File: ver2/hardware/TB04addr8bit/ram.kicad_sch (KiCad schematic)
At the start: 5 parts, among them U29 6116, U32 74AHC04, U40 74HC00, U43 74LS08

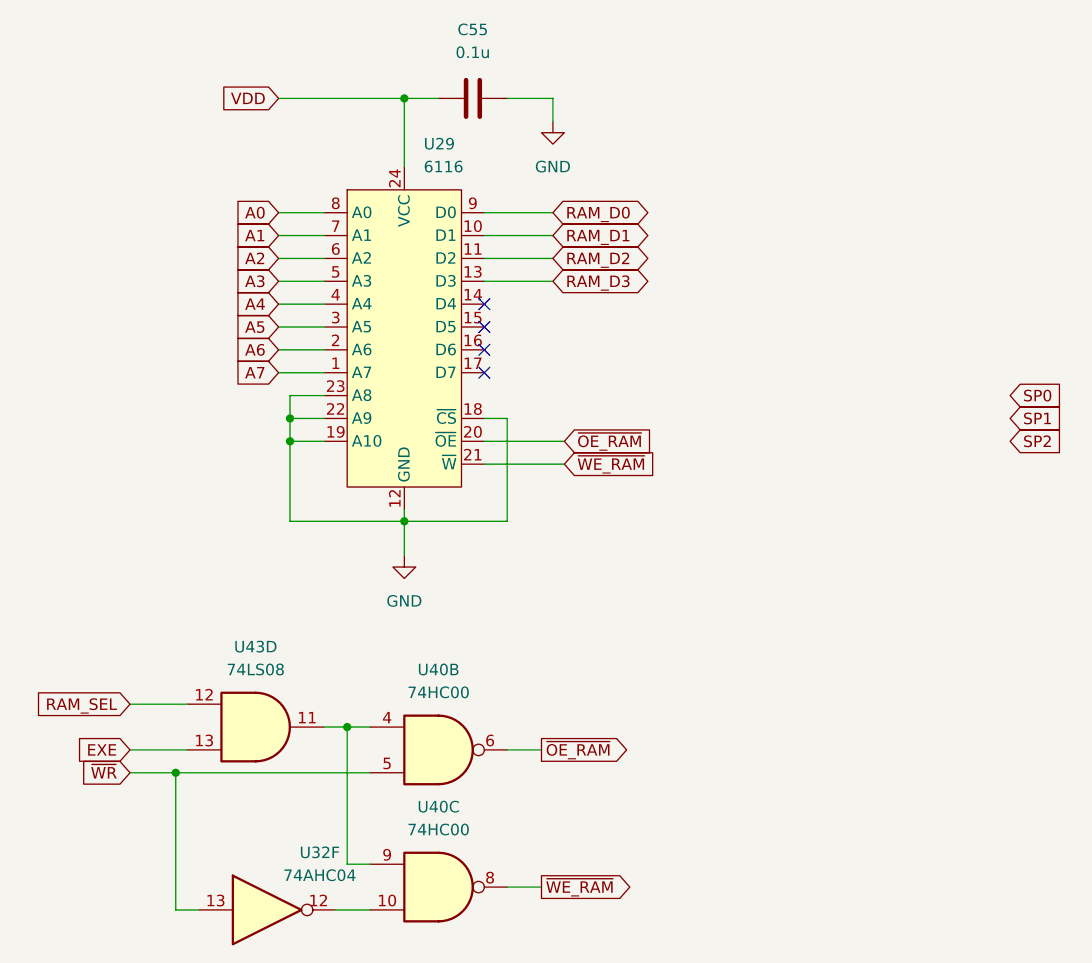
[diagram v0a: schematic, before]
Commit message: ver2: 回路図の要修正5件を修正しアノテーションを掛け直し
- 74HC193(旧U39/新U38)の~CO・~BOをVDD直結から開放に(出力短絡の回避)
- 電源未接続だった4IC(74HC00/74LS32/74AHC04/74LS08)にVCC/GNDを配線
  し、バイパスコンデンサ0.1u×4を追加
- ネット名 Decord を DCR に統一(デコーダ制御信号のラッチ不成立を解消)
- PC_LAOD の綴りを PC_LOAD に修正
- 書込デコーダ138の入力を OPR8-10 から sel_a0-2 へ付け替え
  (LD Ri,[Im8] が別レジスタに書く不具合の解消)
- ver1基板由来だった参照記号をアノテーション掛け直しで整理
  (部品216個・名前付きネット146本とも掛け直し前後で一致、ERCも同数)
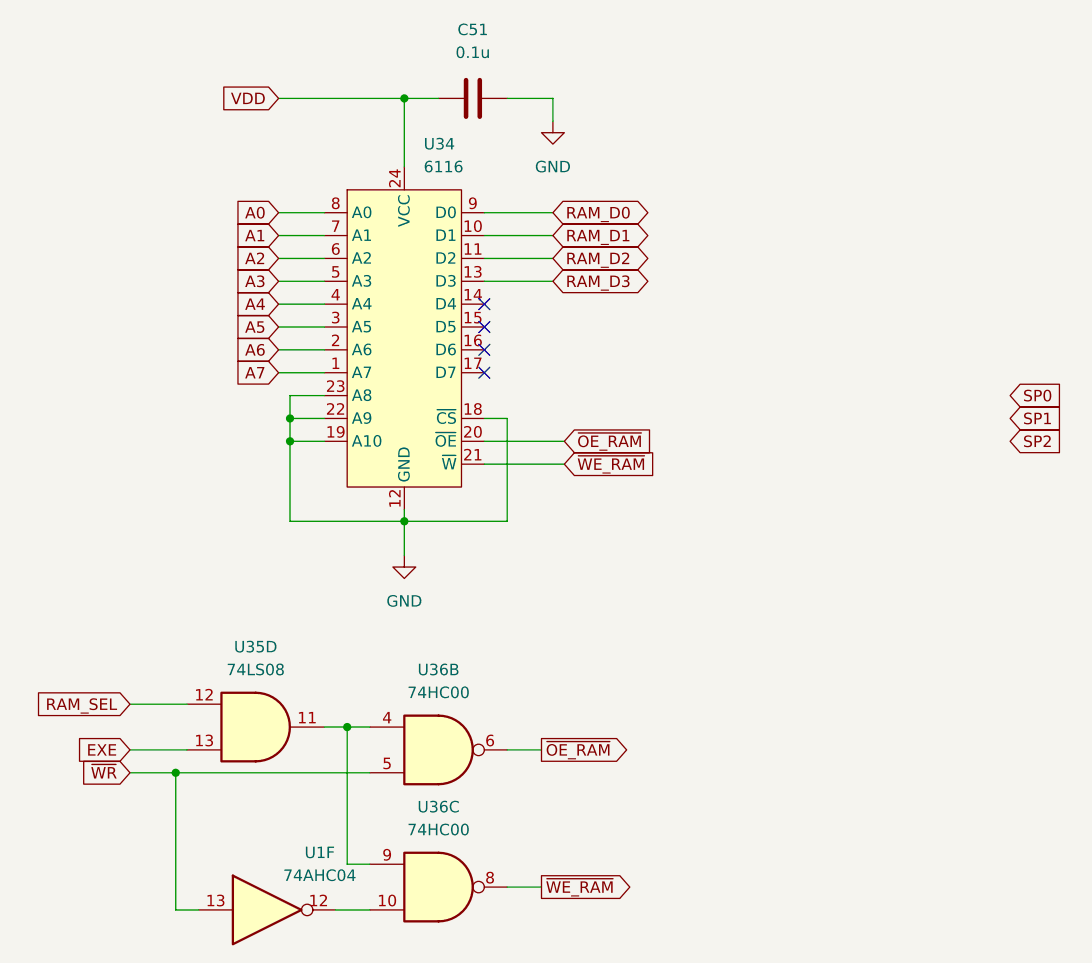
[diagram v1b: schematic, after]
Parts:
- renumbered C55 to C51, U32 to U1, U29 to U34, U43 to U35, U40 to U36
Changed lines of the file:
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@@
 		(dnp no)
 		(fields_autoplaced yes)
-		(property "Reference" "#PWR0121"
+		(property "Reference" "#PWR0124"
 			(at 77.47 87.63 0)
 			(hide yes)
@@
 			(project "TB04addr8bit"
 				(path "/d176c79b-dced-4d01-bcec-7dfd676fcfc2/d4d6bce3-987f-46b3-a9b7-788703d534f1"
-					(reference "#PWR0121")
+					(reference "#PWR0124")
 					(unit 1)
 				)
@@
 		(dnp no)
 		(fields_autoplaced yes)
-		(property "Reference" "U40"
+		(property "Reference" "U36"
 			(at 81.2717 93.98 0)
 			(show_name no)
@@
 			(project "TB04addr8bit"
 				(path "/d176c79b-dced-4d01-bcec-7dfd676fcfc2/d4d6bce3-987f-46b3-a9b7-788703d534f1"
-					(reference "U40")
+					(reference "U36")
 					(unit 2)
 				)
@@
 		(dnp no)
 		(fields_autoplaced yes)
-		(property "Reference" "U43"
+		(property "Reference" "U35"
 			(at 60.9517 91.44 0)
 			(show_name no)
@@
 			(project "TB04addr8bit"
 				(path "/d176c79b-dced-4d01-bcec-7dfd676fcfc2/d4d6bce3-987f-46b3-a9b7-788703d534f1"
-					(reference "U43")
+					(reference "U35")
 					(unit 4)
 				)
@@
 		(dnp no)
 		(fields_autoplaced yes)
-		(property "Reference" "C55"
+		(property "Reference" "C51"
 			(at 85.09 22.86 90)
 			(show_name no)
@@
 			(project "TB04addr8bit"
 				(path "/d176c79b-dced-4d01-bcec-7dfd676fcfc2/d4d6bce3-987f-46b3-a9b7-788703d534f1"
-					(reference "C55")
+					(reference "C51")
 					(unit 1)
 				)
@@
 		(dnp no)
 		(fields_autoplaced yes)
-		(property "Reference" "U29"
+		(property "Reference" "U34"
 			(at 79.6133 35.56 0)
 			(show_name no)
@@
 			(project "TB04addr8bit"
 				(path "/d176c79b-dced-4d01-bcec-7dfd676fcfc2/d4d6bce3-987f-46b3-a9b7-788703d534f1"
-					(reference "U29")
+					(reference "U34")
 					(unit 1)
 				)
@@
 		(dnp no)
 		(fields_autoplaced yes)
-		(property "Reference" "#PWR040"
+		(property "Reference" "#PWR0123"
 			(at 93.98 39.37 0)
 			(hide yes)
@@
 			(project "TB04addr8bit"
 				(path "/d176c79b-dced-4d01-bcec-7dfd676fcfc2/d4d6bce3-987f-46b3-a9b7-788703d534f1"
-					(reference "#PWR040")
+					(reference "#PWR0123")
 					(unit 1)
 				)
@@
 		(in_pos_files yes)
 		(dnp no)
-		(property "Reference" "U32"
+		(property "Reference" "U1"
 			(at 68.072 114.3 0)
 			(show_name no)
@@
 			(project "TB04addr8bit"
 				(path "/d176c79b-dced-4d01-bcec-7dfd676fcfc2/d4d6bce3-987f-46b3-a9b7-788703d534f1"
-					(reference "U32")
+					(reference "U1")
 					(unit 6)
 				)
@@
 		(dnp no)
 		(fields_autoplaced yes)
-		(property "Reference" "U40"
+		(property "Reference" "U36"
 			(at 81.2717 109.22 0)
 			(show_name no)
@@
 			(project "TB04addr8bit"
 				(path "/d176c79b-dced-4d01-bcec-7dfd676fcfc2/d4d6bce3-987f-46b3-a9b7-788703d534f1"
-					(reference "U40")
+					(reference "U36")
 					(unit 3)
 				)
